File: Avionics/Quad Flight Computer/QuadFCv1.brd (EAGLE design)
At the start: 49.5 x 49.5 mm, 122 parts, among them J2 1050270001, Q1 DMP2035U, Q2 DMP2035U, Q3 DMP2035U, SW1 PTS635VL31-VERT, U1 TM4C123GH6PZ, U10 LTC4412, U11 AP7215-33YG-13, U2 74LVC4245APW, U3 ATMEGA32U2-MU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

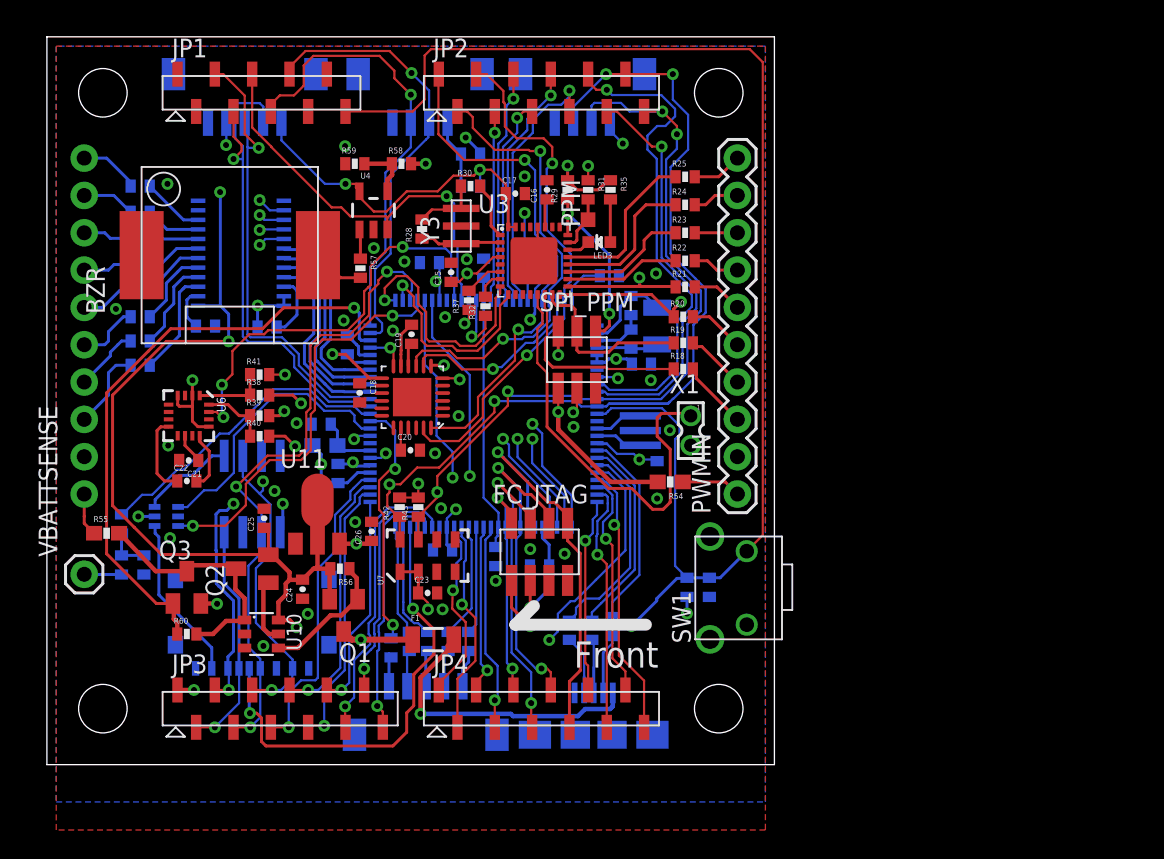
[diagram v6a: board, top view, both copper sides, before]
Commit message: Adjusted FC size to align with power board.
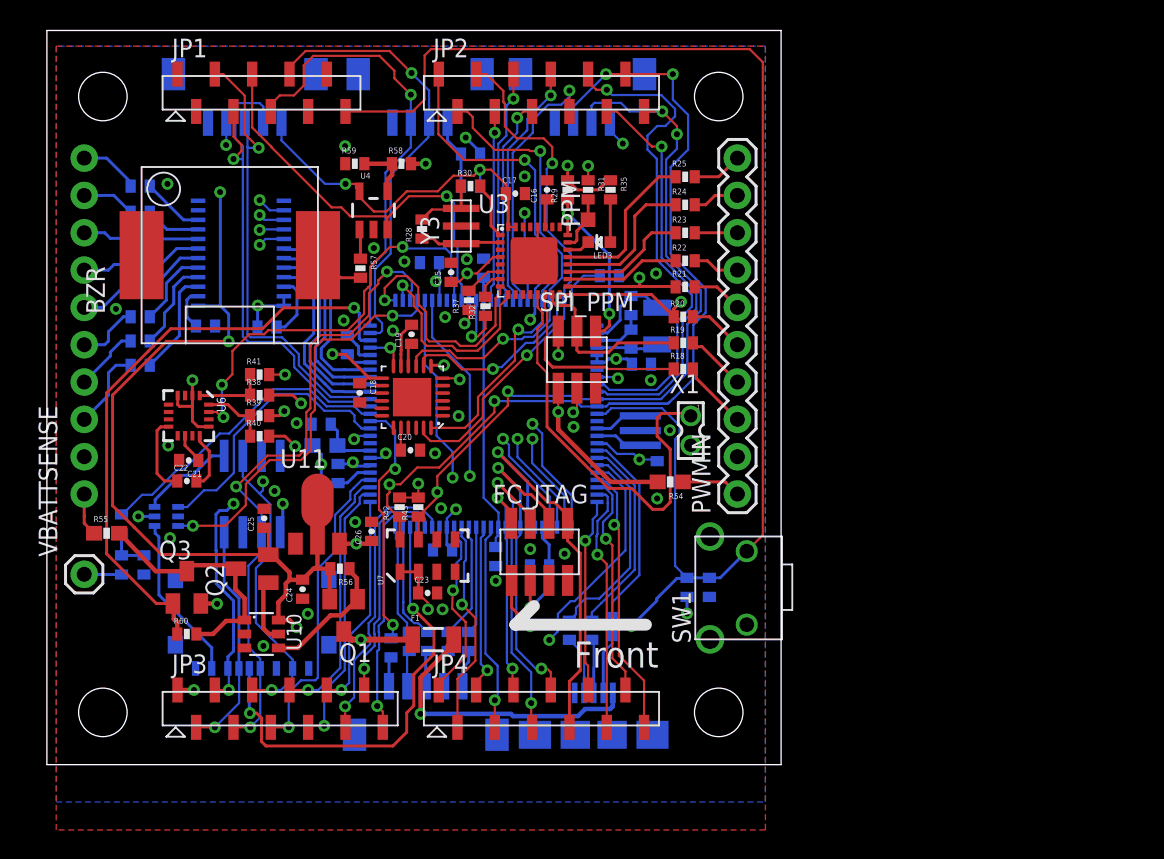
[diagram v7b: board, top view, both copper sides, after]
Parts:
- moved STANDOFF1 0.25 mm to (3.81, 3.56)
- moved STANDOFF3 0.25 mm to (45.7, 3.56)
- moved STANDOFF2 0.25 mm to (3.81, 45.5)
- moved STANDOFF4 0.25 mm to (45.7, 45.5)
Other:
- board size 49.5 x 49.5 mm -> 50 x 50 mm
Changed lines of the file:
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@@
 <board>
 <plain>
-<wire x1="0" y1="0" x2="49.51" y2="0" width="0" layer="20"/>
-<wire x1="49.51" y1="0" x2="49.51" y2="49.53" width="0" layer="20"/>
-<wire x1="49.51" y1="49.53" x2="0" y2="49.53" width="0" layer="20"/>
-<wire x1="0" y1="49.53" x2="0" y2="0" width="0" layer="20"/>
+<wire x1="0" y1="0" x2="49.9618" y2="0" width="0" layer="20"/>
+<wire x1="49.9618" y1="0" x2="49.9618" y2="49.9618" width="0" layer="20"/>
+<wire x1="49.9618" y1="49.9618" x2="0" y2="49.9618" width="0" layer="20"/>
+<wire x1="0" y1="49.9618" x2="0" y2="0" width="0" layer="20"/>
 <wire x1="40.767" y1="9.525" x2="31.877" y2="9.525" width="0.8128" layer="21"/>
 <wire x1="31.877" y1="9.525" x2="33.147" y2="10.795" width="0.8128" layer="21"/>
@@
 <element name="L1" library="QuadFCv1" package="0603" value="10uH" x="18.923" y="21.717" rot="MR0"/>
 <element name="C14" library="QuadFCv1" package="0402-CAP" value="1uF" x="18.669" y="23.1648" rot="MR180"/>
-<element name="STANDOFF1" library="QuadFCv1" package="STAND-OFF" value="STAND-OFF" x="3.81" y="3.81"/>
-<element name="STANDOFF2" library="QuadFCv1" package="STAND-OFF" value="STAND-OFF" x="3.81" y="45.72"/>
-<element name="STANDOFF3" library="QuadFCv1" package="STAND-OFF" value="STAND-OFF" x="45.72" y="3.81"/>
-<element name="STANDOFF4" library="QuadFCv1" package="STAND-OFF" value="STAND-OFF" x="45.72" y="45.72"/>
+<element name="STANDOFF1" library="QuadFCv1" package="STAND-OFF" value="STAND-OFF" x="3.81" y="3.556"/>
+<element name="STANDOFF2" library="QuadFCv1" package="STAND-OFF" value="STAND-OFF" x="3.81" y="45.466"/>
+<element name="STANDOFF3" library="QuadFCv1" package="STAND-OFF" value="STAND-OFF" x="45.72" y="3.556"/>
+<element name="STANDOFF4" library="QuadFCv1" package="STAND-OFF" value="STAND-OFF" x="45.72" y="45.466"/>
 <element name="R18" library="QuadFCv1" package="0402-RES" value="220" x="43.307" y="26.924"/>
 <element name="R19" library="QuadFCv1" package="0402-RES" value="220" x="43.307" y="28.702"/>

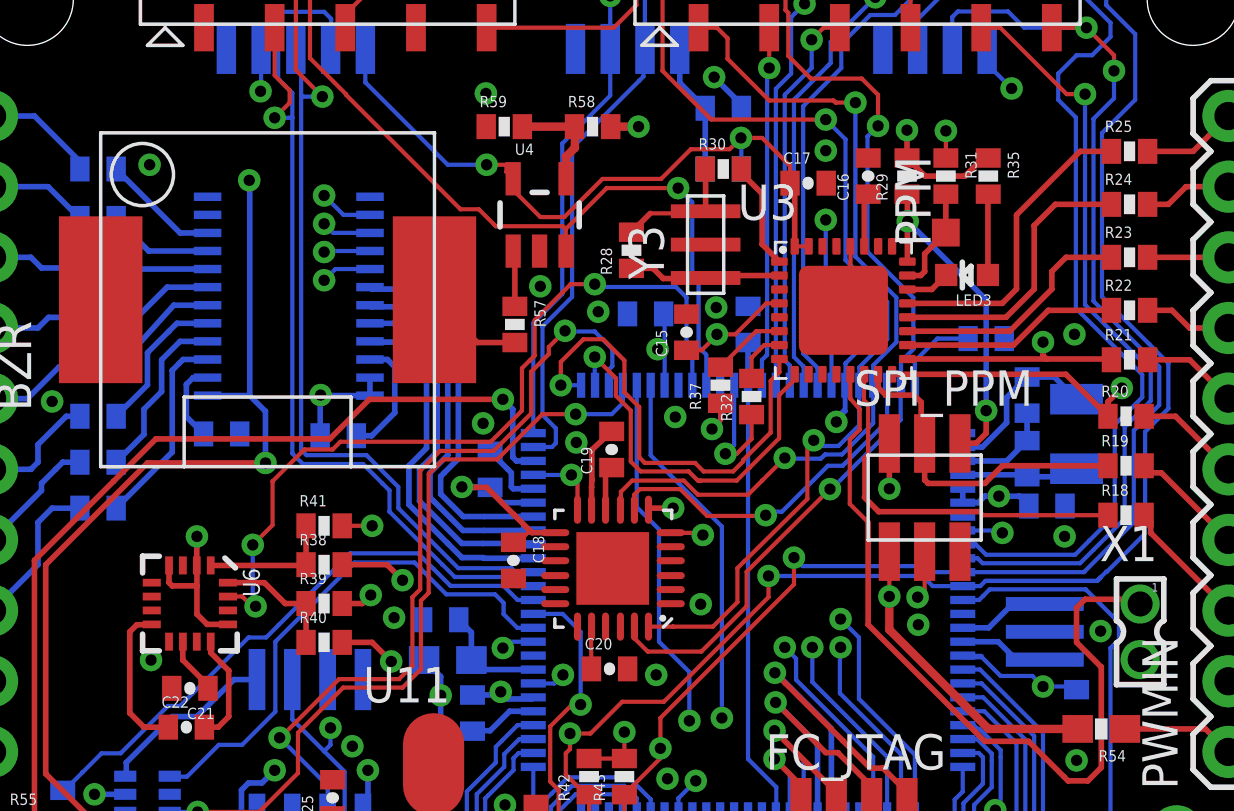
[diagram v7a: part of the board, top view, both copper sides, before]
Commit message: Tracked down the last few airwires
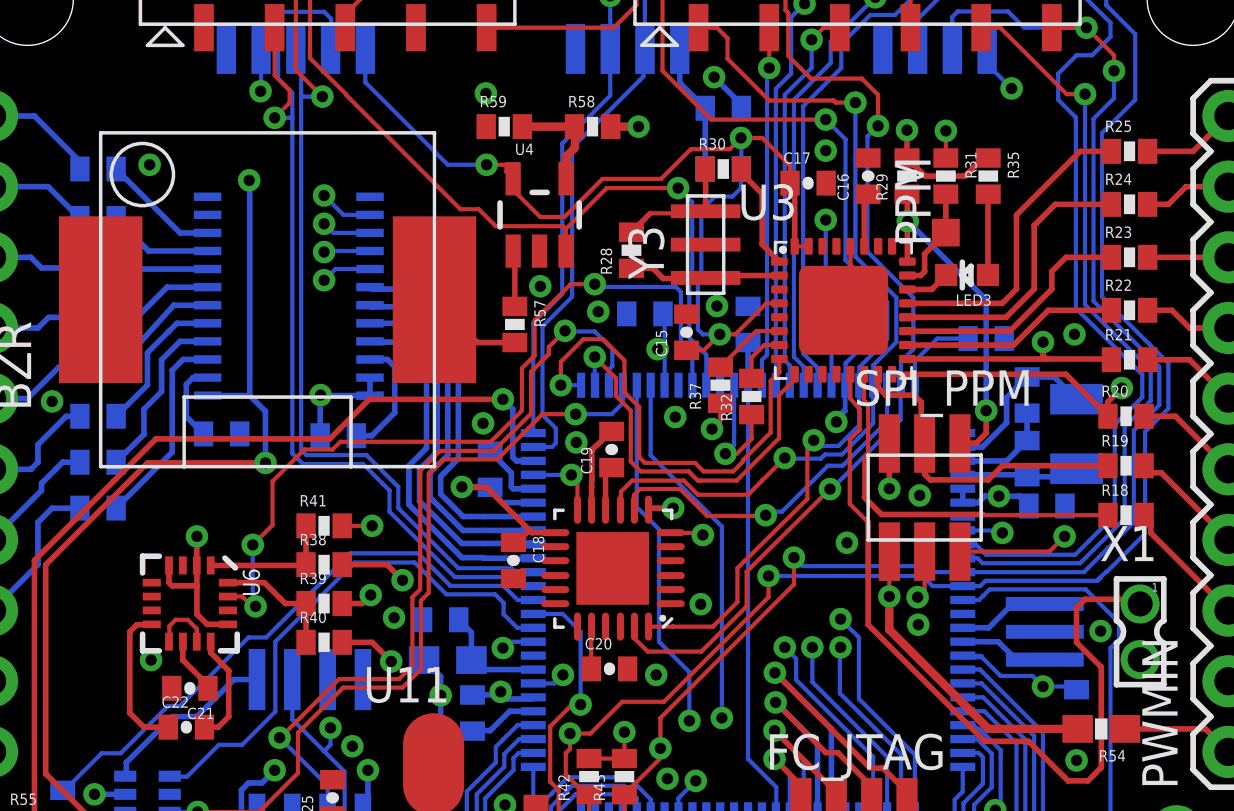
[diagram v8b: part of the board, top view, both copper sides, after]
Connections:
- removed net RXLED: U3.10
- removed net TXLED: U3.11
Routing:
- net 5V: track 143.2 -> 150.7 mm
- net GND: track 18.2 -> 24.4 mm, vias 32 -> 34
- net PWMIN3: track 24.9 -> 25.6 mm
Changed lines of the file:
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@@
 <element name="C13" library="QuadFCv1" package="0402-CAP" value="1uF" x="19.812" y="19.812" rot="MR90"/>
 <element name="C10" library="QuadFCv1" package="0402-CAP" value="0.1uF" x="20.447" y="28.575" rot="MR90"/>
-<element name="C8" library="QuadFCv1" package="0402-CAP" value="0.1uF" x="26.035" y="34.163" rot="MR0"/>
+<element name="C8" library="QuadFCv1" package="0402-CAP" value="0.1uF" x="26.0096" y="34.163" rot="MR0"/>
 <element name="C6" library="QuadFCv1" package="0402-CAP" value="0.1uF" x="33.3756" y="33.8328" rot="MR180"/>
 <element name="C5" library="QuadFCv1" package="0402-CAP" value="0.1uF" x="40.4622" y="27.2542" rot="MR180"/>
@@
 <wire x1="26.718" y1="31.596" x2="26.718" y2="32.9184" width="0.1524" layer="16"/>
 <wire x1="26.718" y1="32.9184" x2="26.718" y2="34.13" width="0.1524" layer="16"/>
-<wire x1="26.718" y1="34.13" x2="26.685" y2="34.163" width="0.1524" layer="16"/>
+<wire x1="26.718" y1="34.13" x2="26.6596" y2="34.163" width="0.1524" layer="16"/>
 <via x="26.4668" y="32.893" extent="1-16" drill="0.4064"/>
 <wire x1="26.4668" y1="32.893" x2="26.6926" y2="32.893" width="0.1524" layer="16"/>
@@
 <via x="41.4528" y="33.4264" extent="1-16" drill="0.4064"/>
 <via x="41.0972" y="26.162" extent="1-16" drill="0.4064"/>
-<via x="28.575" y="34.3916" extent="1-16" drill="0.4064"/>
+<via x="28.6004" y="34.4424" extent="1-16" drill="0.4064"/>
 <via x="27.1018" y="30.4546" extent="1-16" drill="0.4064"/>
 <via x="28.0162" y="23.7236" extent="1-16" drill="0.4064"/>
@@
 <wire x1="33.2232" y1="31.5468" x2="33.2486" y2="31.5722" width="0.1524" layer="16"/>
 <via x="23.5458" y="29.5402" extent="1-16" drill="0.4064"/>
-<wire x1="8.902" y1="22.379" x2="9.902" y2="22.379" width="0" layer="19" extent="1-1"/>
-<wire x1="37.438" y1="26.876" x2="37.338" y2="25.6159" width="0" layer="19" extent="1-16"/>
+<wire x1="37.338" y1="25.6159" x2="40.5511" y2="25.6159" width="0.1524" layer="1"/>
+<wire x1="40.5511" y1="25.6159" x2="41.0972" y2="26.162" width="0.1524" layer="1"/>
+<via x="33.274" y="25.9334" extent="1-16" drill="0.4064"/>
+<via x="35.8902" y="27.6352" extent="1-16" drill="0.4064"/>
+<wire x1="9.902" y1="22.379" x2="9.902" y2="22.8386" width="0.1524" layer="1"/>
+<wire x1="9.902" y1="22.8386" x2="9.5758" y2="23.1648" width="0.1524" layer="1"/>
+<wire x1="9.5758" y1="23.1648" x2="9.144" y2="23.1648" width="0.1524" layer="1"/>
+<wire x1="9.144" y1="23.1648" x2="8.9154" y2="22.9362" width="0.1524" layer="1"/>
+<wire x1="8.9154" y1="22.9362" x2="8.9154" y2="22.3924" width="0.1524" layer="1"/>
+<wire x1="8.9154" y1="22.3924" x2="8.902" y2="22.379" width="0.1524" layer="1"/>
 </signal>
 <signal name="5V">
@@
 <wire x1="7.7978" y1="14.3002" x2="15.0548" y2="14.3002" width="0.2032" layer="1"/>
 <wire x1="15.0548" y1="14.3002" x2="15.07" y2="14.285" width="0.2032" layer="1"/>
-<wire x1="29.2608" y1="33.4264" x2="28.6004" y2="33.4264" width="0.1524" layer="1"/>
-<via x="28.6004" y="33.4264" extent="1-2" drill="0.4064"/>
-<wire x1="28.6004" y1="33.4264" x2="30.734" y2="33.4264" width="0.2032" layer="2"/>
+<wire x1="29.2608" y1="33.4264" x2="28.702" y2="33.4264" width="0.1524" layer="1"/>
+<wire x1="28.702" y1="33.4264" x2="30.734" y2="33.4264" width="0.2032" layer="2"/>
 <wire x1="30.734" y1="33.4264" x2="34.036" y2="30.2006" width="0.2032" layer="2"/>
 <wire x1="34.036" y1="30.2006" x2="34.0614" y2="24.7396" width="0.2032" layer="2"/>
 <wire x1="34.0614" y1="24.7396" x2="34.798" y2="24.003" width="0.2032" layer="2"/>
-<wire x1="28.6004" y1="33.4264" x2="28.6004" y2="33.401" width="0.1524" layer="1"/>
-<wire x1="28.6004" y1="33.401" x2="28.052" y2="32.8526" width="0.1524" layer="1"/>
 <wire x1="11.8046" y1="31.223" x2="11.8046" y2="38.9446" width="0.2032" layer="16"/>
 <wire x1="11.8046" y1="38.9446" x2="11.7856" y2="38.9636" width="0.2032" layer="16"/>
@@
 <wire x1="33.0962" y1="39.3446" x2="30.607" y2="39.3446" width="0.2032" layer="2"/>
 <wire x1="30.607" y1="39.3446" x2="29.464" y2="40.4876" width="0.2032" layer="2"/>
-<wire x1="31.3436" y1="36.5366" x2="30.847" y2="34.54" width="0" layer="19" extent="1-1"/>
+<wire x1="28.0924" y1="33.4264" x2="27.9146" y2="33.6042" width="0.1524" layer="16"/>
+<wire x1="27.9146" y1="33.6042" x2="27.9146" y2="35.306" width="0.1524" layer="16"/>
+<wire x1="27.9146" y1="35.306" x2="28.0416" y2="35.433" width="0.1524" layer="16"/>
+<wire x1="28.0416" y1="35.433" x2="28.0416" y2="37.8968" width="0.1524" layer="16"/>
+<wire x1="28.0416" y1="37.8968" x2="28.5242" y2="38.3794" width="0.1524" layer="16"/>
+<wire x1="28.5242" y1="38.3794" x2="29.1592" y2="38.3794" width="0.1524" layer="16"/>
+<wire x1="29.1592" y1="38.3794" x2="29.464" y2="38.6842" width="0.1524" layer="16"/>
+<wire x1="29.464" y1="38.6842" x2="29.464" y2="39.355" width="0.1524" layer="16"/>
+<wire x1="29.464" y1="39.355" x2="29.479" y2="39.37" width="0.1524" layer="16"/>
+<wire x1="28.0924" y1="33.4264" x2="28.702" y2="33.4264" width="0.1524" layer="16"/>
+<wire x1="28.052" y1="32.8526" x2="28.1282" y2="32.8526" width="0.1524" layer="1"/>
+<wire x1="28.1282" y1="32.8526" x2="28.702" y2="33.4264" width="0.1524" layer="1"/>
+<via x="28.702" y="33.4264" extent="1-16" drill="0.4064"/>
 </signal>
 <signal name="N$1">
@@
 <contactref element="R18" pad="1"/>
 <contactref element="U3" pad="14"/>
-<wire x1="33.897" y1="27.571" x2="34.417" y2="27.051" width="0.2032" layer="1"/>
+<wire x1="33.897" y1="27.571" x2="34.5186" y2="26.9494" width="0.2032" layer="1"/>
 <wire x1="42.53" y1="27.051" x2="42.657" y2="26.924" width="0.2032" layer="1"/>
-<wire x1="34.417" y1="27.051" x2="38.0492" y2="27.051" width="0.2032" layer="1"/>
-<wire x1="38.0492" y1="27.051" x2="38.1762" y2="26.924" width="0.1524" layer="1"/>
+<wire x1="34.5186" y1="26.9494" x2="38.1762" y2="26.9494" width="0.2032" layer="1"/>
+<wire x1="38.1762" y1="26.9494" x2="38.1762" y2="26.924" width="0.1524" layer="1"/>
 <wire x1="42.4792" y1="26.7462" x2="42.657" y2="26.924" width="0.2032" layer="1"/>
 <wire x1="33.897" y1="27.571" x2="33.897" y2="28.9694" width="0.1524" layer="1"/>
@@
 <wire x1="35.941" y1="29.6291" x2="36.068" y2="29.5021" width="0.2032" layer="1"/>
 <wire x1="42.657" y1="28.702" x2="38.862" y2="28.702" width="0.2032" layer="1"/>
-<wire x1="38.862" y1="28.702" x2="38.227" y2="28.067" width="0.2032" layer="1"/>
-<wire x1="38.227" y1="28.067" x2="36.195" y2="28.067" width="0.2032" layer="1"/>
-<wire x1="36.195" y1="28.067" x2="36.068" y2="28.194" width="0.2032" layer="1"/>
-<wire x1="36.068" y1="28.194" x2="36.068" y2="29.5021" width="0.2032" layer="1"/>
+<wire x1="38.862" y1="28.702" x2="38.354" y2="28.194" width="0.2032" layer="1"/>
+<wire x1="38.354" y1="28.194" x2="36.2712" y2="28.194" width="0.2032" layer="1"/>
+<wire x1="36.2712" y1="28.194" x2="36.068" y2="28.3972" width="0.2032" layer="1"/>
+<wire x1="36.068" y1="28.3972" x2="36.068" y2="29.5021" width="0.2032" layer="1"/>
 </signal>
 <signal name="PWMIN3">
@@
 <wire x1="36.068" y1="24.2316" x2="35.814" y2="23.9776" width="0.1524" layer="1"/>
 <via x="35.814" y="23.9776" extent="1-2" drill="0.4064"/>
-<wire x1="35.814" y1="23.9776" x2="35.814" y2="28.4226" width="0.1524" layer="2"/>
 <wire x1="35.814" y1="28.4226" x2="35.814" y2="28.448" width="0.1524" layer="2"/>
 <wire x1="38.8366" y1="31.4706" x2="43.1292" y2="31.4706" width="0.1524" layer="2"/>
@@
 <wire x1="35.814" y1="29.21" x2="38.0746" y2="31.4706" width="0.1524" layer="2"/>
 <wire x1="38.0746" y1="31.4706" x2="38.8366" y2="31.4706" width="0.1524" layer="2"/>
+<wire x1="35.814" y1="28.4226" x2="36.0426" y2="28.4226" width="0.1524" layer="2"/>
+<wire x1="36.0426" y1="28.4226" x2="36.5506" y2="27.9146" width="0.1524" layer="2"/>
+<wire x1="36.5506" y1="27.9146" x2="36.5506" y2="24.7142" width="0.1524" layer="2"/>
+<wire x1="36.5506" y1="24.7142" x2="35.814" y2="23.9776" width="0.1524" layer="2"/>
 </signal>
 <signal name="PWMIN4">
@@
 <wire x1="28.218" y1="31.596" x2="28.218" y2="32.6912" width="0.1524" layer="16"/>
 <wire x1="28.218" y1="32.6912" x2="27.9908" y2="32.9184" width="0.1524" layer="16"/>
-<wire x1="27.9908" y1="32.9184" x2="27.94" y2="32.9692" width="0.1524" layer="16"/>
-<wire x1="27.94" y1="32.9692" x2="27.94" y2="35.3314" width="0.1524" layer="16"/>
-<wire x1="27.94" y1="35.3314" x2="27.7114" y2="35.56" width="0.1524" layer="16"/>
+<wire x1="27.9908" y1="32.9184" x2="27.6098" y2="33.2994" width="0.1524" layer="16"/>
+<wire x1="27.6098" y1="33.2994" x2="27.6098" y2="35.433" width="0.1524" layer="16"/>
+<wire x1="27.6098" y1="35.433" x2="27.7114" y2="35.56" width="0.1524" layer="16"/>
 <wire x1="27.7114" y1="35.56" x2="27.7114" y2="38.1762" width="0.1524" layer="16"/>
 <wire x1="27.7114" y1="38.1762" x2="27.2034" y2="38.6842" width="0.1524" layer="16"/>
@@
 <wire x1="28.1178" y1="37.776" x2="28.194" y2="37.8522" width="0.1524" layer="1"/>
 </signal>
-<signal name="RXLED">
-<contactref element="U3" pad="10"/>
-</signal>
-<signal name="TXLED">
-<contactref element="U3" pad="11"/>
-</signal>
 <signal name="XT1R">
 <contactref element="U3" pad="1"/>
@@
 <contactref element="U1" pad="34"/>
 <wire x1="27.718" y1="31.596" x2="27.718" y2="32.6832" width="0.1524" layer="16"/>
-<wire x1="27.718" y1="32.6832" x2="27.5082" y2="32.893" width="0.1524" layer="16"/>
-<wire x1="27.5082" y1="32.893" x2="27.5082" y2="34.7472" width="0.1524" layer="16"/>
-<wire x1="27.5082" y1="34.7472" x2="27.1272" y2="35.1282" width="0.1524" layer="16"/>
+<wire x1="27.718" y1="32.6832" x2="27.305" y2="33.0962" width="0.1524" layer="16"/>
+<wire x1="27.305" y1="33.0962" x2="27.305" y2="34.9504" width="0.1524" layer="16"/>
+<wire x1="27.305" y1="34.9504" x2="27.1272" y2="35.1282" width="0.1524" layer="16"/>
 <wire x1="27.1272" y1="35.1282" x2="24.3078" y2="35.1282" width="0.1524" layer="16"/>
 <wire x1="24.3078" y1="35.1282" x2="24.2062" y2="35.2298" width="0.1524" layer="16"/>
